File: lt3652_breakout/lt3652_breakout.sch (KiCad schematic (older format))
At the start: 35 parts, among them CON1 SLR PNL, U1 LT3652

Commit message: WIP on Rev 0.2
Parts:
- removed CON1: SLR PNL, Connect:JACK_ALIM, symbol BARREL_JACK
- added Pslr1: JST PH, w_conn_jst-ph:b2b-ph-kl, symbol CONN_01X02
- C3, Cvin2: footprint Capacitors_SMD:C_0603_HandSoldering -> Capacitors_SMD:C_1206_HandSoldering
- Ctmr1: renamed from C1; value C_Small -> 0.68µF
- Cvfbat1: value 20pF -> 22pF
- Rsense1: footprint Resistors_SMD:R_0603_HandSoldering -> Capacitors_SMD:C_0805_HandSoldering
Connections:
- net GND: now also Pslr1.2 (P2)
- net at Dvin1.3 (A), RV1.1, RV2.1: now also Pslr1.1 (P1)
- no-connect marks 5 -> 4
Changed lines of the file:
@@
 F 0 "Cvin2" H 4275 2925 50  0000 L CNN
 F 1 "10uF" H 4275 2725 50  0000 L CNN
-F 2 "Capacitors_SMD:C_0603_HandSoldering" H 4288 2675 50  0001 C CNN
+F 2 "Capacitors_SMD:C_1206_HandSoldering" H 4288 2675 50  0001 C CNN
 F 3 "" H 4250 2825 50  0000 C CNN
 	1    4250 2825
@@
 $EndComp
 $Comp
-L BARREL_JACK CON1
-U 1 1 56C2A4EA
-P 4825 2000
-F 0 "CON1" H 4825 2250 50  0000 C CNN
-F 1 "SLR PNL" H 4825 1800 50  0000 C CNN
-F 2 "Connect:JACK_ALIM" H 4825 2000 50  0001 C CNN
-F 3 "" H 4825 2000 50  0000 C CNN
-	1    4825 2000
-	0    1    1    0
-$EndComp
-$Comp
 L GND #PWR04
 U 1 1 56C2A92A
@@
 	1    0    0    -1
 $EndComp
-NoConn ~ 4825 2300
 $Comp
 L PWR_FLAG #FLG05
@@
 F 0 "C3" H 6110 4095 50  0000 L CNN
 F 1 "10uF" H 6110 3945 39  0000 L CNN
-F 2 "Capacitors_SMD:C_0603_HandSoldering" H 6100 4025 50  0001 C CNN
+F 2 "Capacitors_SMD:C_1206_HandSoldering" H 6100 4025 50  0001 C CNN
 F 3 "" H 6100 4025 50  0000 C CNN
 	1    6100 4025
@@
 	4250 2975 4250 3050
 Wire Wire Line
-	4725 2300 4725 2425
+	4725 2235 4725 2425
 Wire Wire Line
 	4250 2675 4250 2375
@@
 $EndComp
 Wire Wire Line
-	7850 3150 7250 3150
+	7250 3150 7850 3150
 Wire Wire Line
 	7250 2390 7250 3550
@@
 $EndComp
 Wire Wire Line
-	7800 3400 7800 3250
+	7800 3250 7800 3400
 Wire Wire Line
 	7800 3250 7850 3250
@@
 P 6350 3700
 F 0 "Cvfbat1" H 6360 3770 50  0000 L CNN
-F 1 "20pF" V 6250 3550 50  0000 L CNN
+F 1 "22pF" V 6250 3550 50  0000 L CNN
 F 2 "Capacitors_SMD:C_0603_HandSoldering" H 6350 3700 50  0001 C CNN
 F 3 "" H 6350 3700 50  0000 C CNN
@@
 F 0 "Rsense1" H 6680 3420 50  0000 L CNN
 F 1 "250mO" H 6680 3360 50  0000 L CNN
-F 2 "Resistors_SMD:R_0603_HandSoldering" H 6650 3400 50  0001 C CNN
+F 2 "Capacitors_SMD:C_0805_HandSoldering" H 6650 3400 50  0001 C CNN
 F 3 "" H 6650 3400 50  0000 C CNN
 	1    6650 3400
@@
 	3465 4655 3360 4655
 $Comp
-L C_Small C1
+L C_Small Ctmr1
 U 1 1 56D0C26A
 P 4230 4700
-F 0 "C1" H 4240 4770 50  0000 L CNN
-F 1 "C_Small" H 4240 4620 50  0000 L CNN
+F 0 "Ctmr1" H 4240 4770 50  0000 L CNN
+F 1 "0.68µF" H 4240 4620 50  0000 L CNN
 F 2 "Capacitors_SMD:C_0603_HandSoldering" H 4230 4700 50  0001 C CNN
 F 3 "" H 4230 4700 50  0000 C CNN
@@
 $EndComp
 Wire Wire Line
-	4925 2625 4925 2300
+	4925 2145 4925 2625
 Wire Wire Line
 	4100 2610 4925 2610
@@
 $EndComp
 Connection ~ 7250 2440
+$Comp
+L CONN_01X02 Pslr1
+U 1 1 56D5EAF0
+P 4875 1945
+F 0 "Pslr1" H 4875 2095 50  0000 C CNN
+F 1 "JST PH" V 4975 1945 50  0000 C CNN
+F 2 "w_conn_jst-ph:b2b-ph-kl" H 4875 1945 50  0001 C CNN
+F 3 "" H 4875 1945 50  0000 C CNN
+	1    4875 1945
+	0    1    -1   0
+$EndComp
+Wire Wire Line
+	4825 2145 4825 2235
+Wire Wire Line
+	4825 2235 4725 2235
 $EndSCHEMATC

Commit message: Relaid pcb to the size of the box that will house it
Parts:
- D1, D2: footprint LEDs:LED_0603 -> LEDs:LED-3MM
- Dbatbst1: footprint Diodes_ThroughHole:Diode_DO-35_SOD27_Horizontal_RM10 -> Diodes_ThroughHole:Diode_DO-41_SOD81_Vertical_AnodeUp
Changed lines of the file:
@@
 F 0 "D1" H 2630 4135 39  0000 L CNN
 F 1 "3mm GRN" H 2605 4060 39  0000 L CNN
-F 2 "LEDs:LED_0603" V 2755 4185 50  0001 C CNN
+F 2 "LEDs:LED-3MM" V 2755 4185 50  0001 C CNN
 F 3 "" V 2755 4185 50  0000 C CNN
 	1    2755 4185
@@
 F 0 "D2" H 2630 4555 39  0000 L CNN
 F 1 "3mm RED" H 2605 4705 39  0000 L CNN
-F 2 "LEDs:LED_0603" V 2755 4605 50  0001 C CNN
+F 2 "LEDs:LED-3MM" V 2755 4605 50  0001 C CNN
 F 3 "" V 2755 4605 50  0000 C CNN
 	1    2755 4605
@@
 F 0 "Dbatbst1" H 6200 3280 50  0000 L CNN
 F 1 "D_Small" H 6100 3120 50  0000 L CNN
-F 2 "Diodes_ThroughHole:Diode_DO-35_SOD27_Horizontal_RM10" V 6250 3200 50  0001 C CNN
+F 2 "Diodes_ThroughHole:Diode_DO-41_SOD81_Vertical_AnodeUp" V 6250 3200 50  0001 C CNN
 F 3 "" V 6250 3200 50  0000 C CNN
 	1    6250 3200

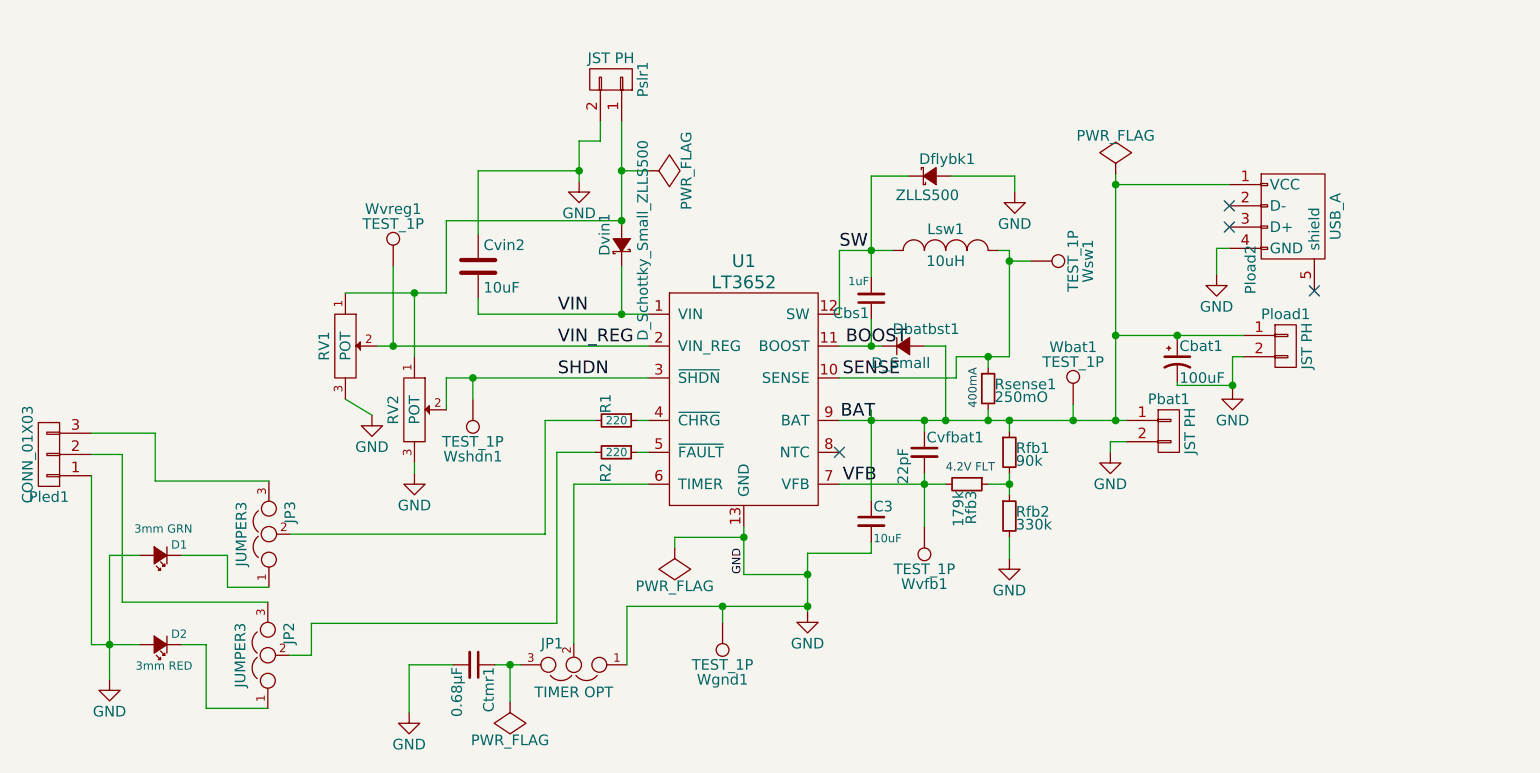
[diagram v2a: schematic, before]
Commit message: Added option to connect load directly to Vin. Also routed the PCB
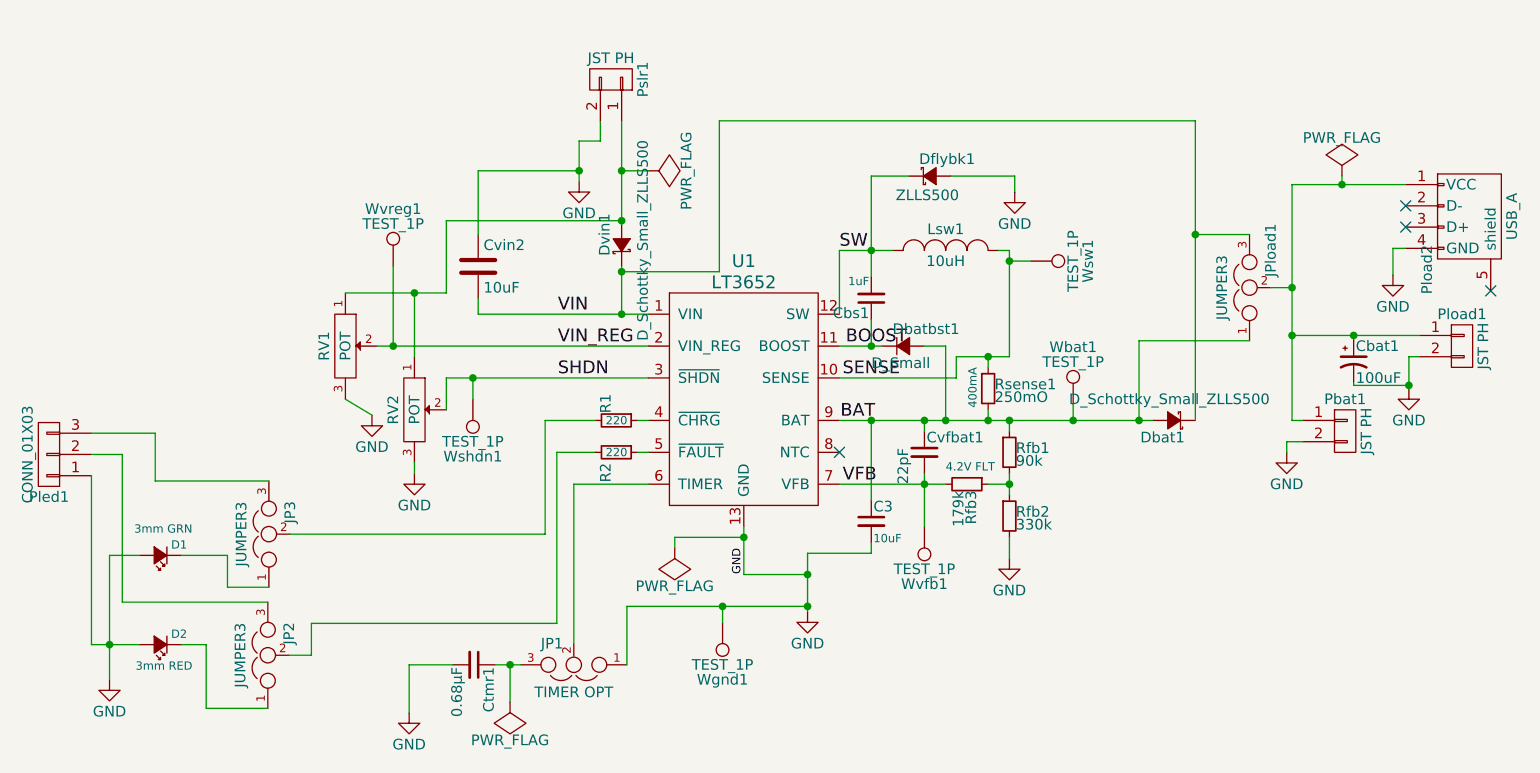
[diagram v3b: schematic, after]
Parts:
- added Dbat1: D_Schottky_Small_ZLLS500, diodes:DIODES_INC_ZLLS500, symbol D_Schottky_Small_ZLLS500
- added JPload1: JUMPER3, Pin_Headers:Pin_Header_Straight_1x03, symbol JUMPER3
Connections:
- net BAT: now also Dbat1.3 (A), JPload1.1; no longer Cbat1.1, Pbat1.1 (P1), Pload1.1 (P1), Pload2.1 (VCC)
- net VIN: now also Dbat1.1 (K), JPload1.3
- new net: Cbat1.1, JPload1.2, Pbat1.1 (P1), Pload1.1 (P1), Pload2.1 (VCC)
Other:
- moved on the sheet: Cbat1, Pbat1, Pload1, Pload2
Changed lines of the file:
@@
 	5175 4100 5500 4100
 Connection ~ 5500 4100
-Wire Wire Line
-	6100 3500 6100 3925
 Connection ~ 5800 4275
 $Comp
@@
 L GND #PWR09
 U 1 1 56C670F4
-P 7225 3700
-F 0 "#PWR09" H 7225 3450 50  0001 C CNN
-F 1 "GND" H 7225 3550 50  0000 C CNN
-F 2 "" H 7225 3700 50  0000 C CNN
-F 3 "" H 7225 3700 50  0000 C CNN
-	1    7225 3700
+P 8055 3700
+F 0 "#PWR09" H 8055 3450 50  0001 C CNN
+F 1 "GND" H 8055 3550 50  0000 C CNN
+F 2 "" H 8055 3700 50  0000 C CNN
+F 3 "" H 8055 3700 50  0000 C CNN
+	1    8055 3700
 	1    0    0    -1
 $EndComp
@@
 L CONN_01X02 Pbat1
 U 1 1 56CB9AD3
-P 7500 3600
-F 0 "Pbat1" H 7500 3750 50  0000 C CNN
-F 1 "JST PH" V 7600 3600 50  0000 C CNN
-F 2 "w_conn_jst-ph:b2b-ph-kl" H 7500 3600 50  0001 C CNN
-F 3 "" H 7500 3600 50  0000 C CNN
-	1    7500 3600
-	1    0    0    -1
-$EndComp
-Wire Wire Line
-	7225 3700 7225 3650
-Wire Wire Line
-	7225 3650 7300 3650
+P 8330 3600
+F 0 "Pbat1" H 8330 3750 50  0000 C CNN
+F 1 "JST PH" V 8430 3600 50  0000 C CNN
+F 2 "w_conn_jst-ph:b2b-ph-kl" H 8330 3600 50  0001 C CNN
+F 3 "" H 8330 3600 50  0000 C CNN
+	1    8330 3600
+	1    0    0    -1
+$EndComp
+Wire Wire Line
+	8055 3700 8055 3650
+Wire Wire Line
+	8055 3650 8130 3650
 Wire Wire Line
 	5950 3050 5950 2750
@@
 Wire Wire Line
 	5950 3200 6150 3200
-Wire Wire Line
-	5950 3550 7300 3550
 Connection ~ 6100 3550
 Wire Wire Line
@@
 L CONN_01X02 Pload1
 U 1 1 56CF675B
-P 8050 3200
-F 0 "Pload1" H 8050 3350 50  0000 C CNN
-F 1 "JST PH" V 8150 3200 50  0000 C CNN
-F 2 "w_conn_jst-ph:b2b-ph-kl" H 8050 3200 50  0001 C CNN
-F 3 "" H 8050 3200 50  0000 C CNN
-	1    8050 3200
-	1    0    0    -1
-$EndComp
-Wire Wire Line
-	7250 3150 7850 3150
-Wire Wire Line
-	7250 2390 7250 3550
-Connection ~ 7250 3550
+P 8880 3200
+F 0 "Pload1" H 8880 3350 50  0000 C CNN
+F 1 "JST PH" V 8980 3200 50  0000 C CNN
+F 2 "w_conn_jst-ph:b2b-ph-kl" H 8880 3200 50  0001 C CNN
+F 3 "" H 8880 3200 50  0000 C CNN
+	1    8880 3200
+	1    0    0    -1
+$EndComp
+Wire Wire Line
+	8080 3150 8680 3150
 $Comp
 L GND #PWR012
 U 1 1 56CF694F
-P 7800 3400
-F 0 "#PWR012" H 7800 3150 50  0001 C CNN
-F 1 "GND" H 7800 3250 50  0000 C CNN
-F 2 "" H 7800 3400 50  0000 C CNN
-F 3 "" H 7800 3400 50  0000 C CNN
-	1    7800 3400
-	1    0    0    -1
-$EndComp
-Wire Wire Line
-	7800 3250 7800 3400
-Wire Wire Line
-	7800 3250 7850 3250
+P 8630 3400
+F 0 "#PWR012" H 8630 3150 50  0001 C CNN
+F 1 "GND" H 8630 3250 50  0000 C CNN
+F 2 "" H 8630 3400 50  0000 C CNN
+F 3 "" H 8630 3400 50  0000 C CNN
+	1    8630 3400
+	1    0    0    -1
+$EndComp
+Wire Wire Line
+	8630 3250 8630 3400
+Wire Wire Line
+	8630 3250 8680 3250
 Text Notes 6450 3800 0    39   ~ 0
 4.2V FLT
@@
 L CP1_Small Cbat1
 U 1 1 56D1522A
-P 7540 3270
-F 0 "Cbat1" H 7550 3340 50  0000 L CNN
-F 1 "100uF" H 7550 3190 50  0000 L CNN
-F 2 "Capacitors_ThroughHole:C_Radial_D5_L6_P2.5" H 7540 3270 50  0001 C CNN
-F 3 "" H 7540 3270 50  0000 C CNN
-	1    7540 3270
-	1    0    0    -1
-$EndComp
-Wire Wire Line
-	7540 3370 7540 3385
-Wire Wire Line
-	7540 3385 7800 3385
-Connection ~ 7800 3385
+P 8370 3270
+F 0 "Cbat1" H 8380 3340 50  0000 L CNN
+F 1 "100uF" H 8380 3190 50  0000 L CNN
+F 2 "Capacitors_ThroughHole:C_Radial_D5_L6_P2.5" H 8370 3270 50  0001 C CNN
+F 3 "" H 8370 3270 50  0000 C CNN
+	1    8370 3270
+	1    0    0    -1
+$EndComp
+Wire Wire Line
+	8370 3370 8370 3385
+Wire Wire Line
+	8370 3385 8630 3385
+Connection ~ 8630 3385
 $Comp
 L USB_A Pload2
 U 1 1 56D16751
-P 8085 2640
-F 0 "Pload2" H 8285 2440 50  0000 C CNN
-F 1 "USB_A" H 8035 2840 50  0000 C CNN
-F 2 "connectors:WURTH_ELEKTRONIK_629104151021" V 8035 2540 50  0001 C CNN
-F 3 "" V 8035 2540 50  0000 C CNN
-	1    8085 2640
+P 8915 2640
+F 0 "Pload2" H 9115 2440 50  0000 C CNN
+F 1 "USB_A" H 8865 2840 50  0000 C CNN
+F 2 "connectors:WURTH_ELEKTRONIK_629104151021" V 8865 2540 50  0001 C CNN
+F 3 "" V 8865 2540 50  0000 C CNN
+	1    8915 2640
 	0    1    1    0
 $EndComp
@@
 L GND #PWR014
 U 1 1 56D16B0E
-P 7725 2865
-F 0 "#PWR014" H 7725 2615 50  0001 C CNN
-F 1 "GND" H 7725 2715 50  0000 C CNN
-F 2 "" H 7725 2865 50  0000 C CNN
-F 3 "" H 7725 2865 50  0000 C CNN
-	1    7725 2865
-	1    0    0    -1
-$EndComp
-Wire Wire Line
-	7725 2865 7725 2740
-Wire Wire Line
-	7725 2740 7785 2740
-NoConn ~ 7785 2540
-NoConn ~ 7785 2640
-NoConn ~ 8185 2940
-Connection ~ 7250 3150
-Wire Wire Line
-	7540 3170 7540 3150
-Connection ~ 7540 3150
-Wire Wire Line
-	7250 2440 7785 2440
-$Comp
-L PWR_FLAG #FLG015
-U 1 1 56D19FA8
-P 7250 2390
-F 0 "#FLG015" H 7250 2485 50  0001 C CNN
-F 1 "PWR_FLAG" H 7250 2570 50  0000 C CNN
-F 2 "" H 7250 2390 50  0000 C CNN
-F 3 "" H 7250 2390 50  0000 C CNN
-	1    7250 2390
-	1    0    0    -1
-$EndComp
-Connection ~ 7250 2440
+P 8555 2865
+F 0 "#PWR014" H 8555 2615 50  0001 C CNN
+F 1 "GND" H 8555 2715 50  0000 C CNN
+F 2 "" H 8555 2865 50  0000 C CNN
+F 3 "" H 8555 2865 50  0000 C CNN
+	1    8555 2865
+	1    0    0    -1
+$EndComp
+Wire Wire Line
+	8555 2865 8555 2740
+Wire Wire Line
+	8555 2740 8615 2740
+NoConn ~ 8615 2540
+NoConn ~ 8615 2640
+NoConn ~ 9015 2940
+Connection ~ 8080 3150
+Wire Wire Line
+	8370 3170 8370 3150
+Connection ~ 8370 3150
+Wire Wire Line
+	8080 2440 8615 2440
 $Comp
 L CONN_01X02 Pslr1
@@
 Wire Wire Line
 	4825 2235 4725 2235
+$Comp
+L D_Schottky_Small_ZLLS500 Dbat1
+U 1 1 56D71C0A
+P 7525 3550
+F 0 "Dbat1" H 7475 3630 50  0000 L CNN
+F 1 "D_Schottky_Small_ZLLS500" H 7075 3450 50  0000 L CNN
+F 2 "diodes:DIODES_INC_ZLLS500" V 7525 3550 50  0001 C CNN
+F 3 "" V 7525 3550 50  0000 C CNN
+	1    7525 3550
+	-1   0    0    1
+$EndComp
+Wire Wire Line
+	7425 3550 5950 3550
+Wire Wire Line
+	6100 3925 6100 3550
+Wire Wire Line
+	4925 2850 5385 2850
+Wire Wire Line
+	5385 2850 5385 2140
+Connection ~ 4925 2850
+$Comp
+L JUMPER3 JPload1
+U 1 1 56D774FB
+P 7880 2925
+F 0 "JPload1" H 7930 2825 50  0000 L CNN
+F 1 "JUMPER3" H 7880 3025 50  0000 C BNN
+F 2 "Pin_Headers:Pin_Header_Straight_1x03" H 7880 2925 50  0001 C CNN
+F 3 "" H 7880 2925 50  0000 C CNN
+	1    7880 2925
+	0    -1   -1   0
+$EndComp
+Wire Wire Line
+	7980 2925 8080 2925
+Connection ~ 8080 2925
+Wire Wire Line
+	8080 3550 8130 3550
+Wire Wire Line
+	7360 3550 7360 3175
+Wire Wire Line
+	7360 3175 7880 3175
+Connection ~ 7360 3550
+Wire Wire Line
+	7625 3550 7625 2140
+Wire Wire Line
+	7625 2140 5385 2140
+Wire Wire Line
+	7880 2675 7625 2675
+Connection ~ 7625 2675
+Wire Wire Line
+	8080 2440 8080 3550
+$Comp
+L PWR_FLAG #FLG015
+U 1 1 56D7B958
+P 8315 2400
+F 0 "#FLG015" H 8315 2495 50  0001 C CNN
+F 1 "PWR_FLAG" H 8315 2580 50  0000 C CNN
+F 2 "" H 8315 2400 50  0000 C CNN
+F 3 "" H 8315 2400 50  0000 C CNN
+	1    8315 2400
+	1    0    0    -1
+$EndComp
+Wire Wire Line
+	8315 2400 8315 2440
+Connection ~ 8315 2440
 $EndSCHEMATC
